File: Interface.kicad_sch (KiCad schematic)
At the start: 29 parts, among them U11 WE-TVS-82400102, U2 SN74LVC2G14DBV, U6 THVD1400D, U7 TLP2310, U8 TLP2310

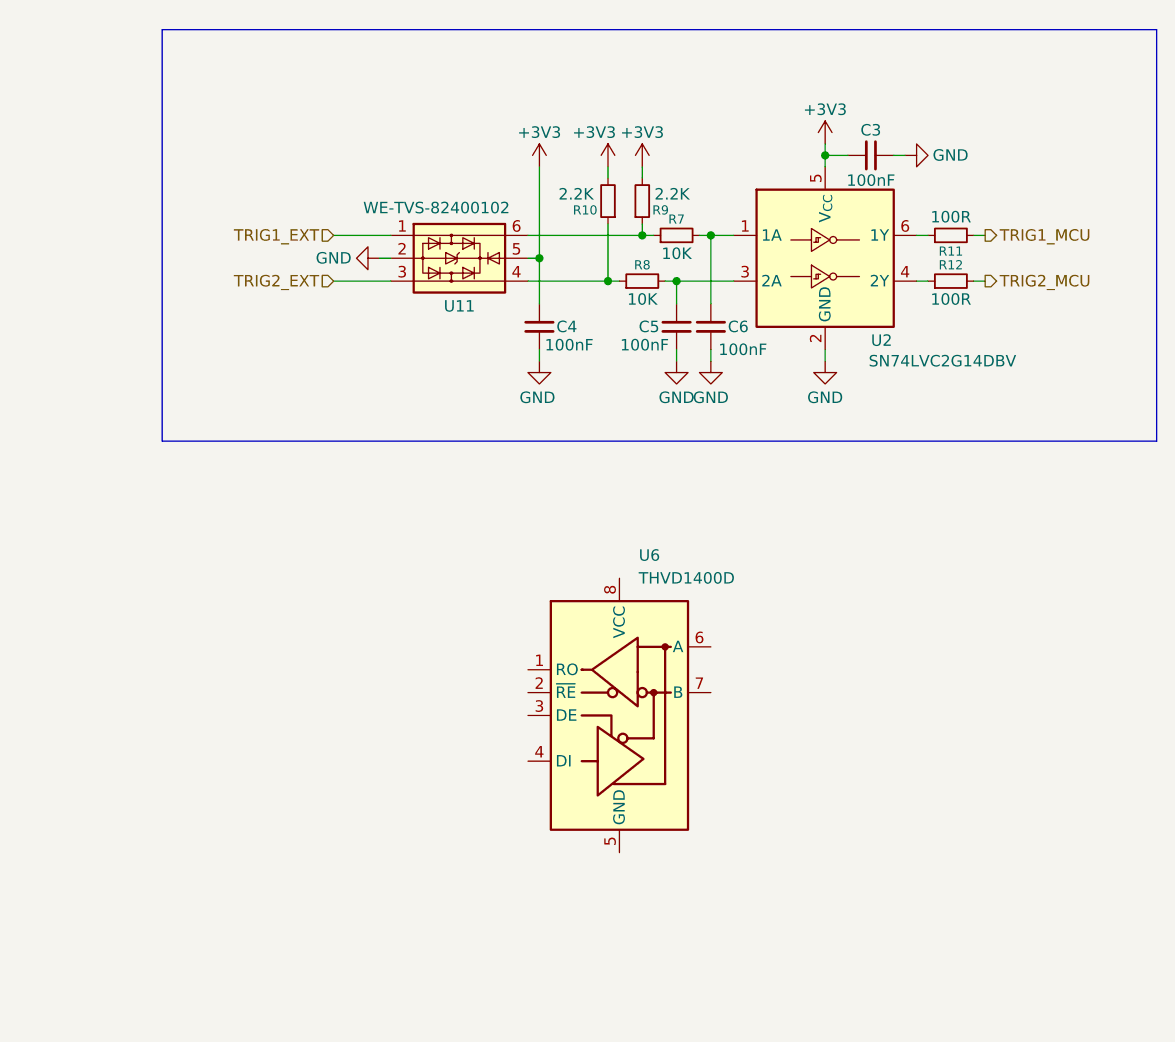
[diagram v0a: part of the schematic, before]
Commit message: git commit -m "Add RS485 transceiver circuitry"
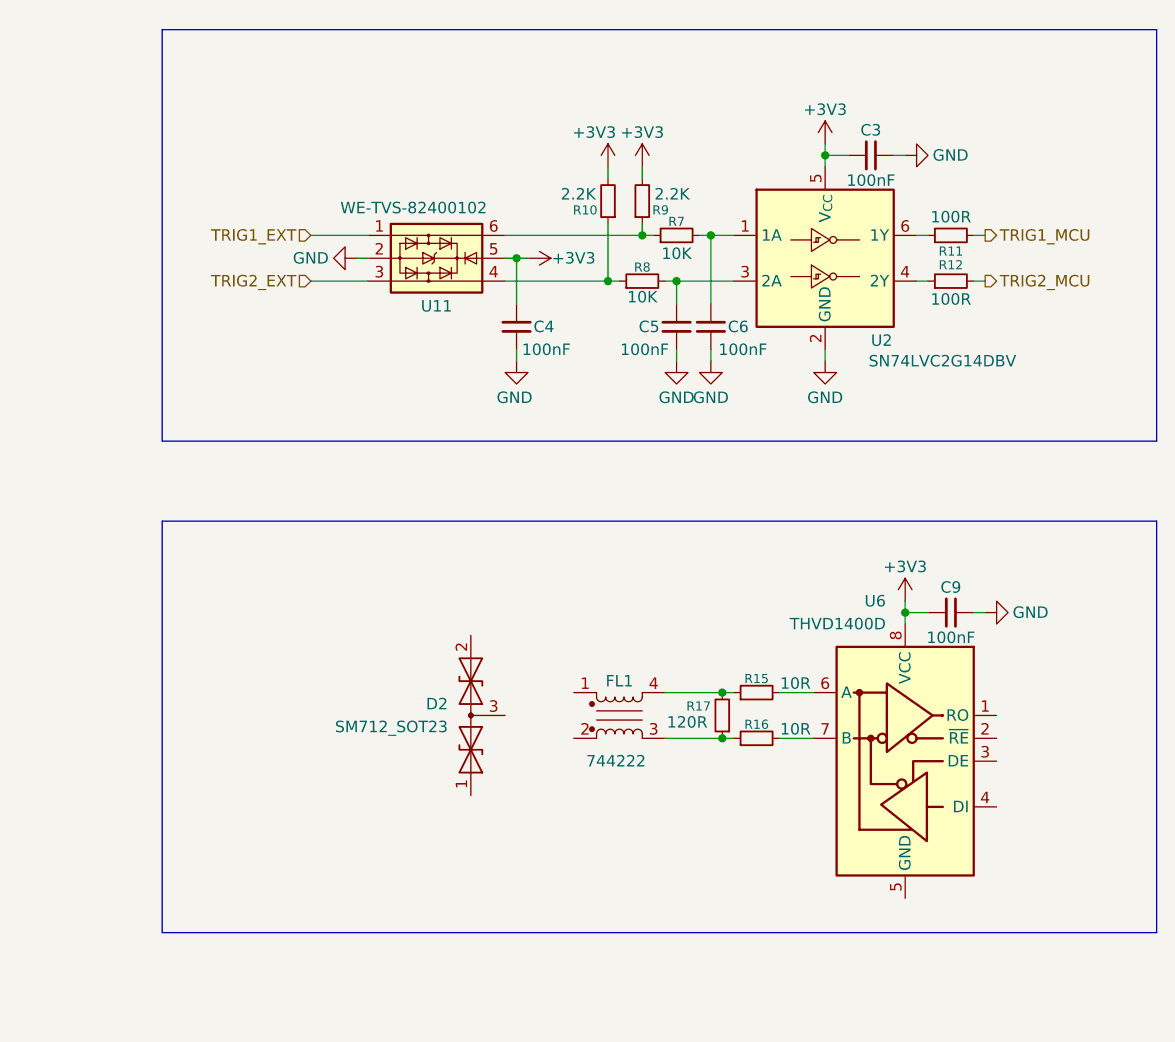
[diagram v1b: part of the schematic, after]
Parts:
- added C9: 100nF, Capacitor_SMD:C_0603_1608Metric, symbol Device:C_Small
- added D2: SM712_SOT23, Package_TO_SOT_SMD:SOT-23, symbol Diode:SM712_SOT23
- added FL1: 744222, symbol Device:Filter_EMI_LL_1423
- added R15, R16: 10R, Resistor_SMD:R_0603_1608Metric, symbol Device:R_Small
- added R17: 120R, Resistor_SMD:R_0603_1608Metric, symbol Device:R_Small
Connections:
- net +3V3: now also U6.8 (VCC), C9.1
- net GND: now also C9.2
- net at U6.6 (A): now also R15.2
- net at U6.7 (B): now also R16.2
- new net: FL1.3, R16.1, R17.1
- new net: FL1.4, R15.1, R17.2
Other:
- moved on the sheet: U11, U6

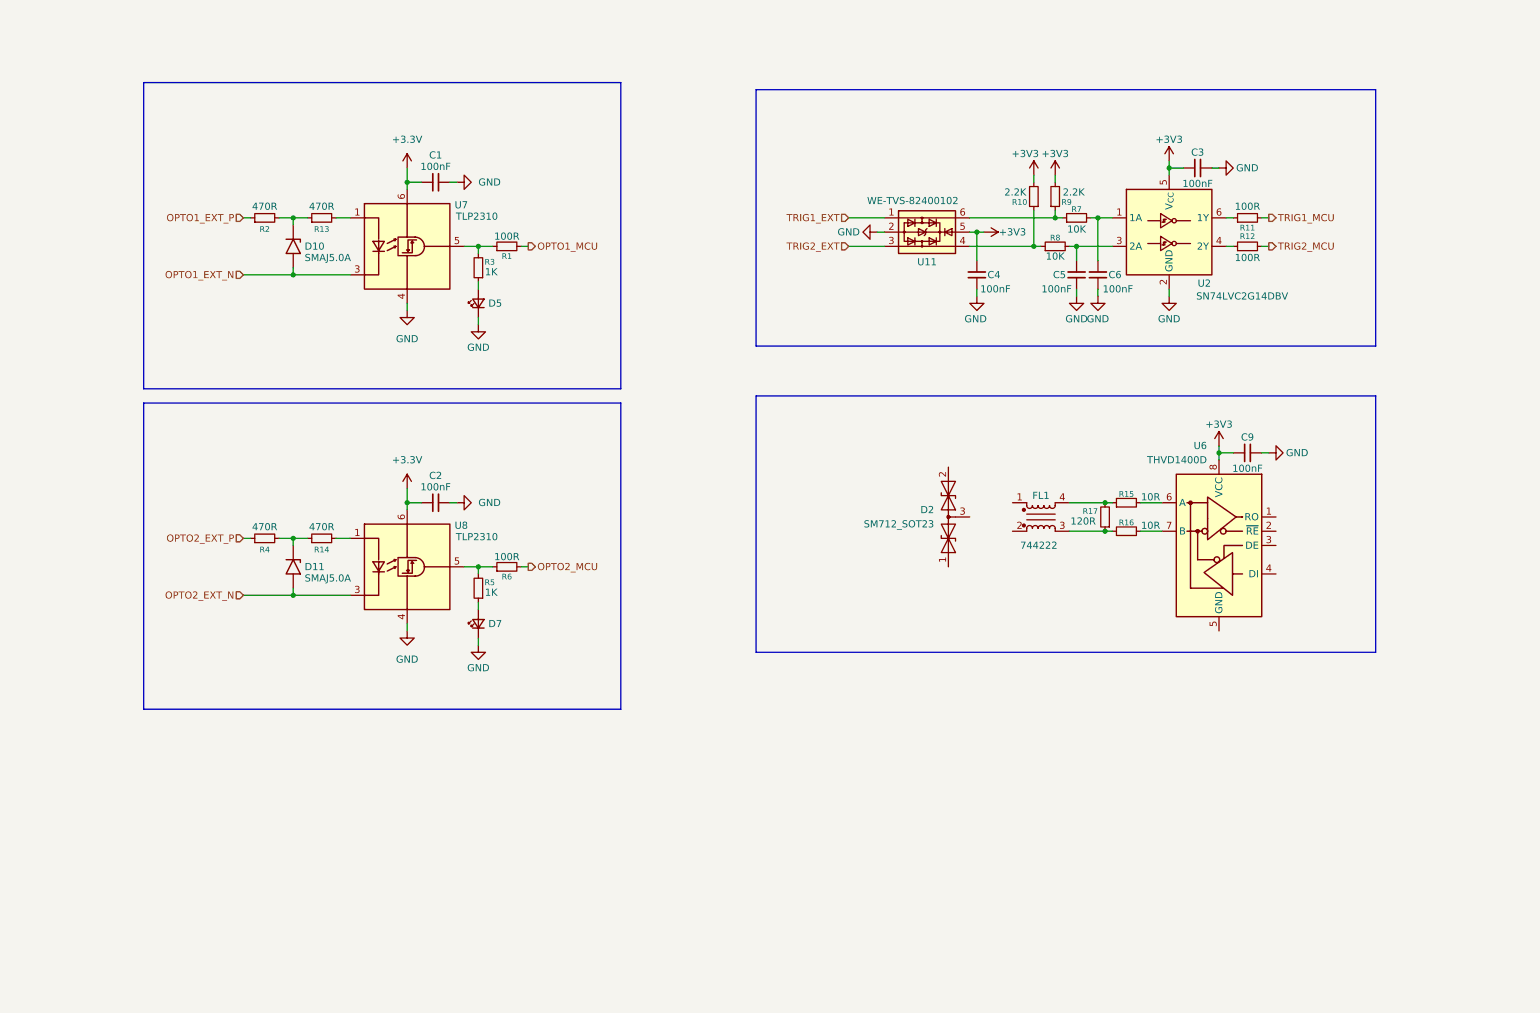
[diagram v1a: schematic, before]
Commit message: Update schematics: limit switches, debug TC2070 and power supply stage
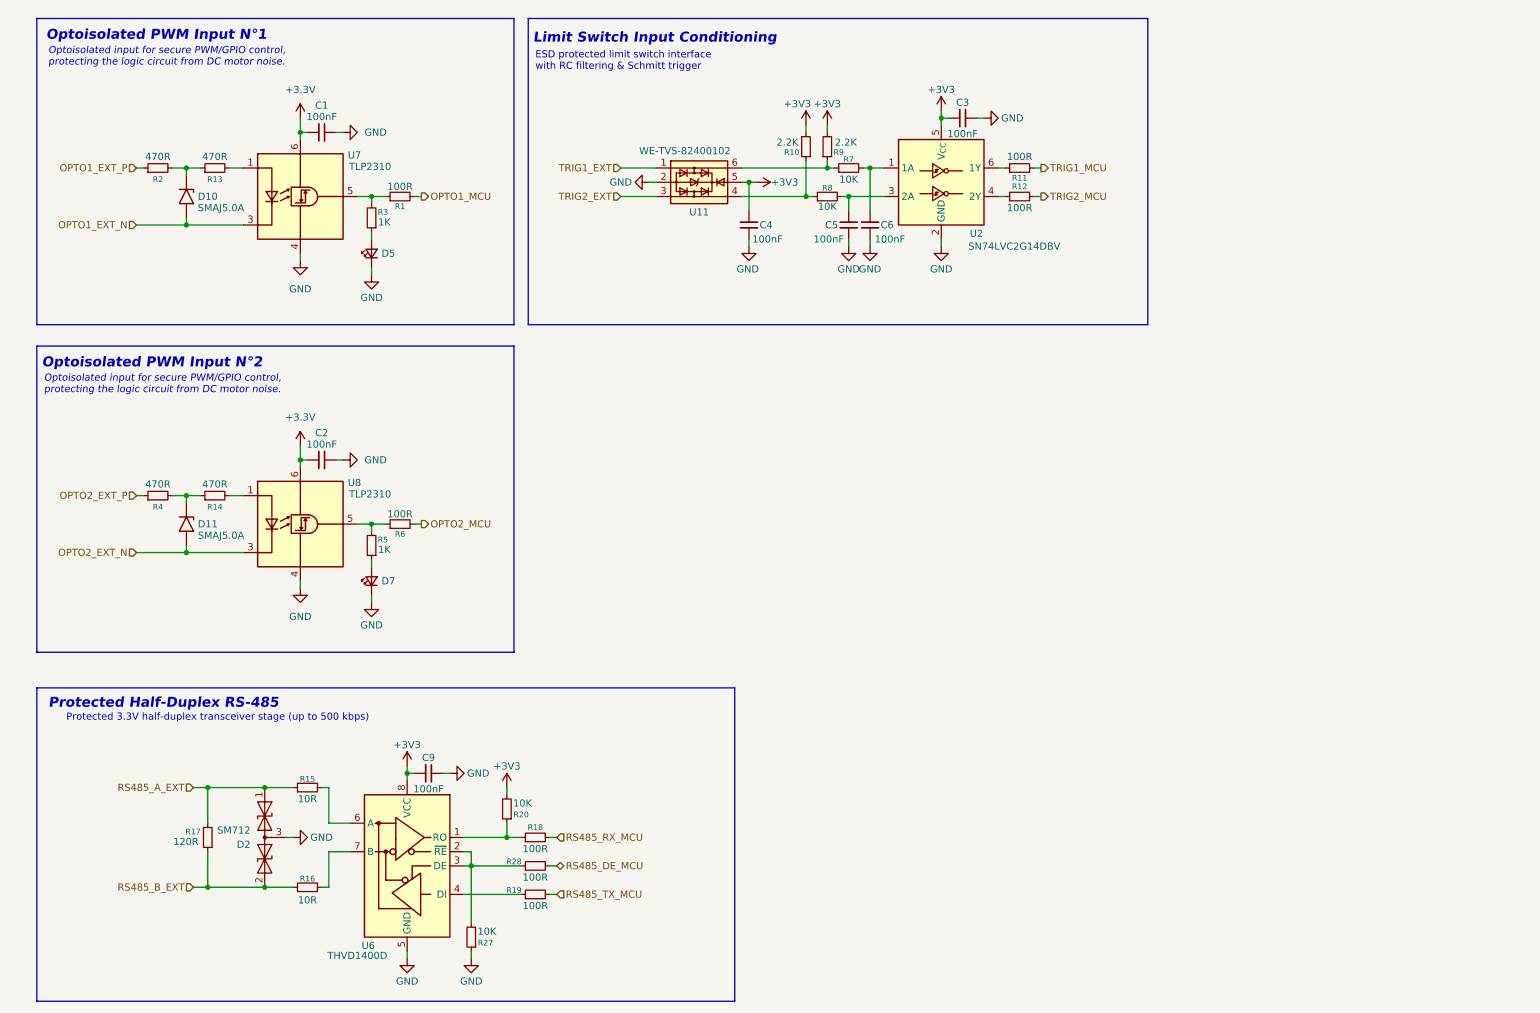
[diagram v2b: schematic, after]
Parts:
- removed FL1: 744222, symbol Device:Filter_EMI_LL_1423
- added R18, R19, R28: 100R, Resistor_SMD:R_0603_1608Metric, symbol Device:R_Small
- added R20, R27: 10K, Resistor_SMD:R_0603_1608Metric, symbol Device:R_Small
- D2: value SM712_SOT23 -> SM712
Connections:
- net +3V3: now also R20.2
- net GND: now also D2.3 (common), U6.5 (GND), R27.1
- net RS485_A_EXT: now reaches D2.1 (A1)
- net RS485_A_EXT: now also R15.1, R17.2
- net RS485_B_EXT: now reaches D2.2 (A2)
- net RS485_B_EXT: now also R16.1, R17.1
- net at U6.1 (RO): now also R18.1, R20.1
- net at U6.2 (~{RE}): now also U6.3 (DE), R27.2, R28.1
- net at U6.4 (DI): now also R19.1
- new net RS485_DE_MCU: R28.2
- new net RS485_RX_MCU: R18.2
- new net RS485_TX_MCU: R19.2
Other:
- note added: "ESD protected limit switch interface with RC filtering & Schmitt trigger"
- note added: "Limit Switch Input Conditioning"
- note added: "Optoisolated PWM Input N°1"
- note added: "Optoisolated PWM Input N°2"
- note added: "Optoisolated input for secure PWM/GPIO control, protecting the logic circuit from DC motor noise."
- note added: "Protected 3.3V half-duplex transceiver stage (up to 500 kbps)"
- note added: "Protected Half-Duplex RS-485"
- moved on the sheet: C1, C2, C3, C4, C5, C6, C9, D10, D11, D2, D5, D7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

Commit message: feat(lib): initialize local project library and 3D step models
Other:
- title: KinetiCoreDC -> KinetiCoreDC - Interface
- moved on the sheet: C2, C3, C4, C5, C6, C9, D11, D2, D7, R10, R11, R12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

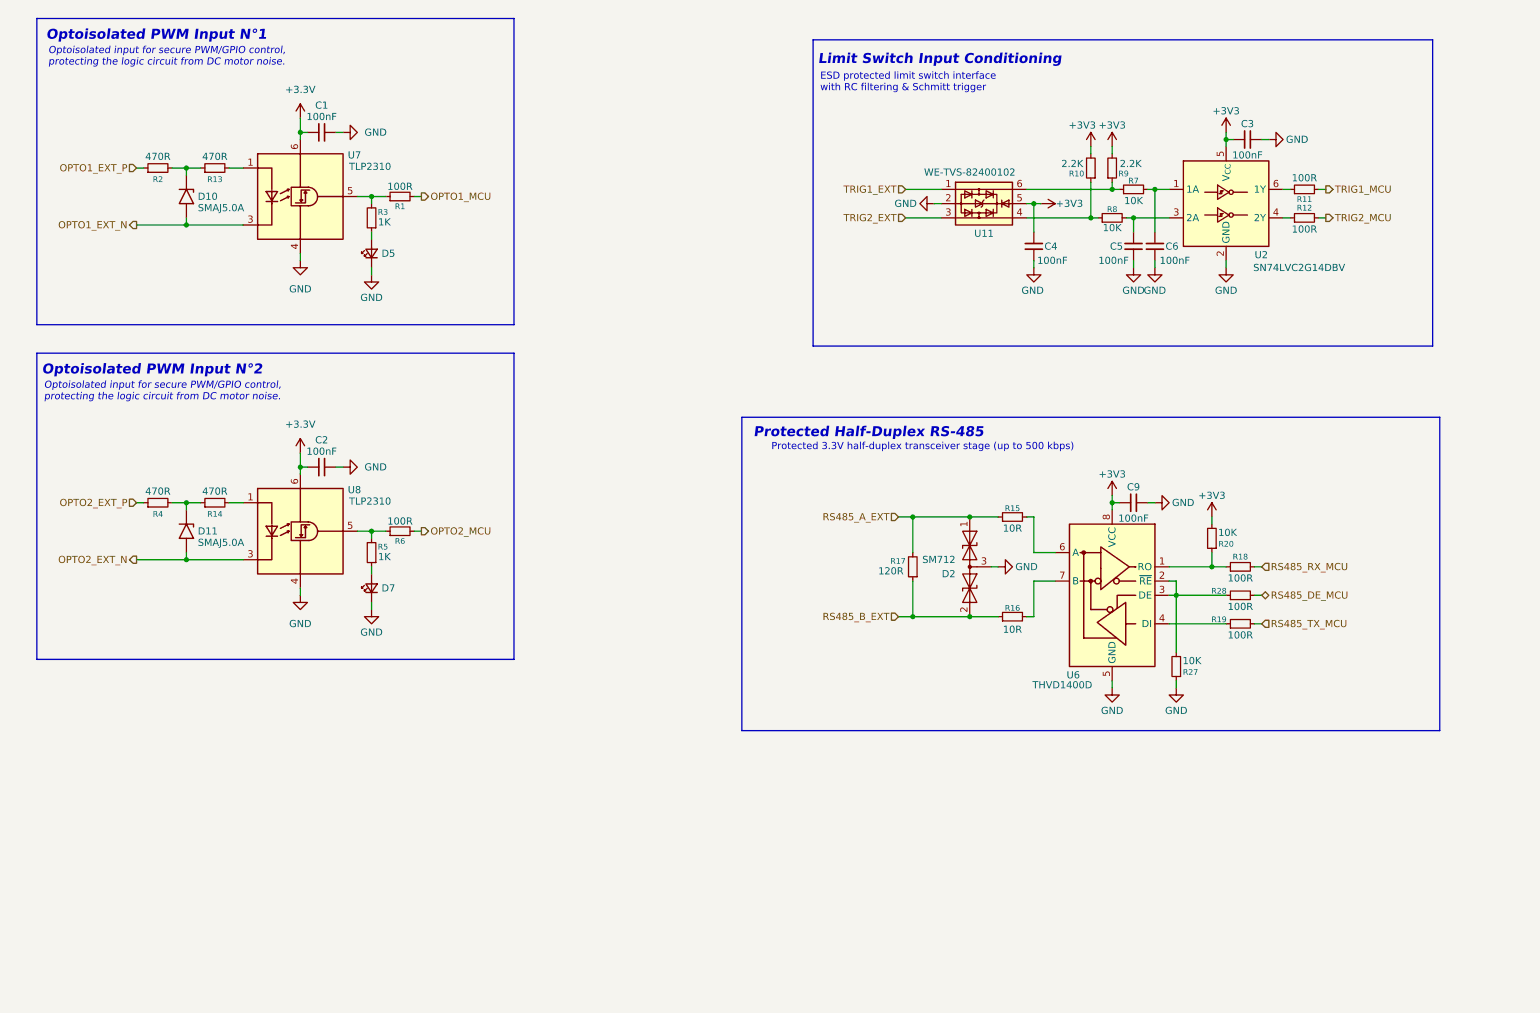
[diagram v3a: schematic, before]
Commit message: feat: add driver component and some correction
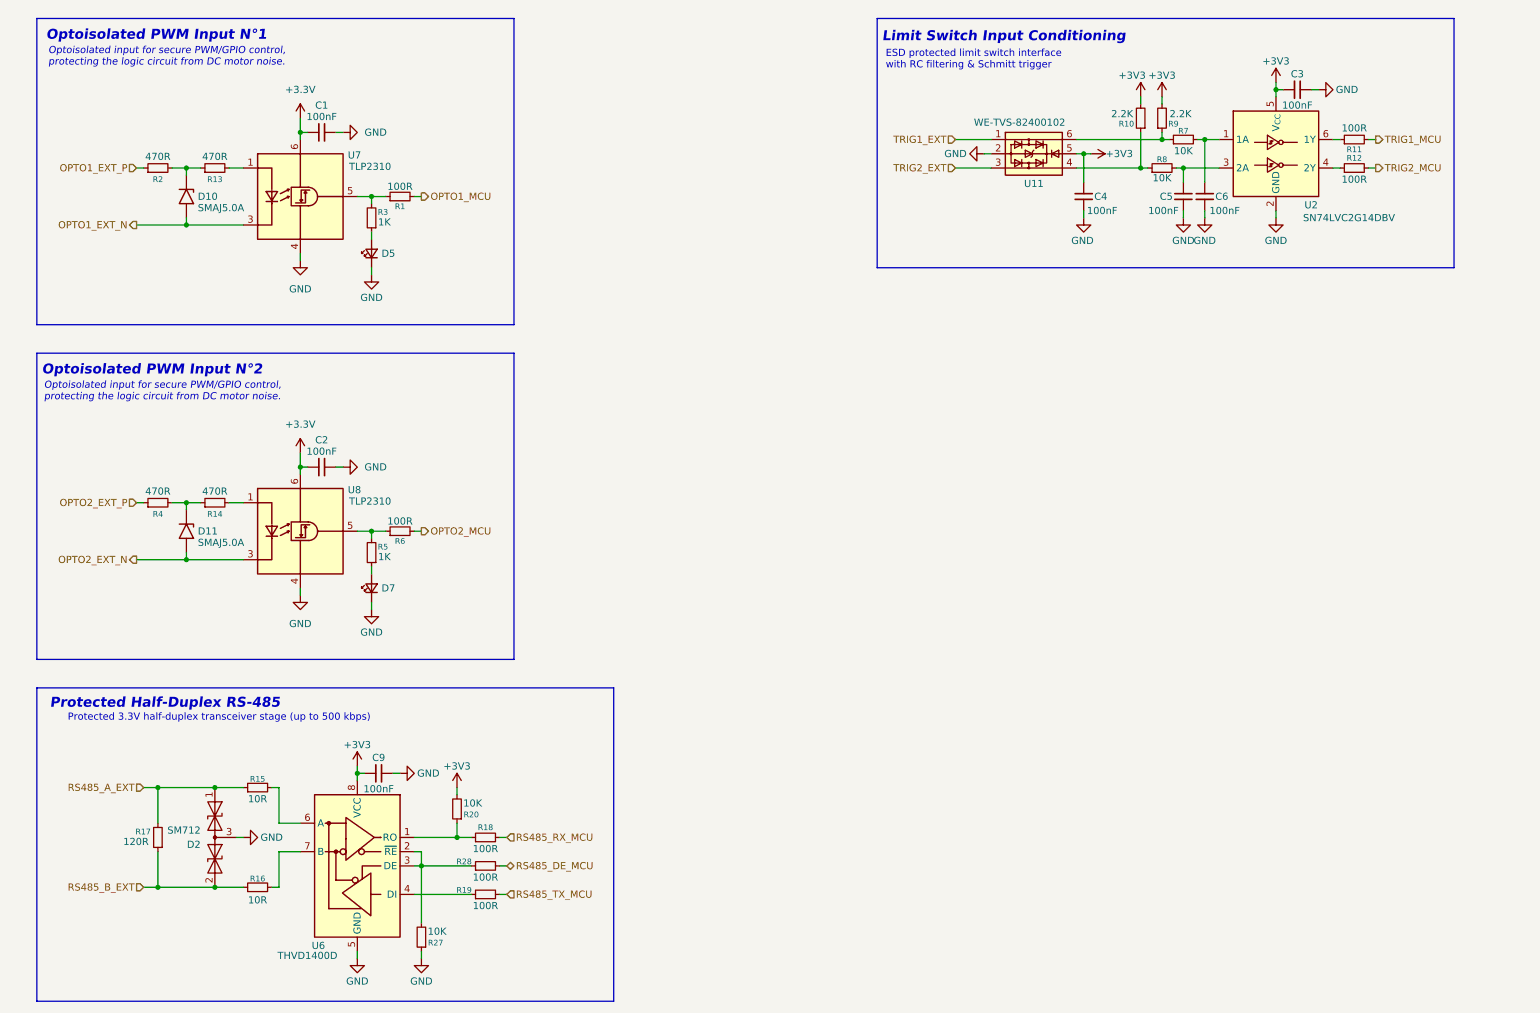
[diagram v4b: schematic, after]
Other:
- moved on the sheet: C3, C4, C5, C6, C9, D2, R10, R11, R12, R15, R16, R17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
